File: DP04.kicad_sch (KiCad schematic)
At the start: 26 parts

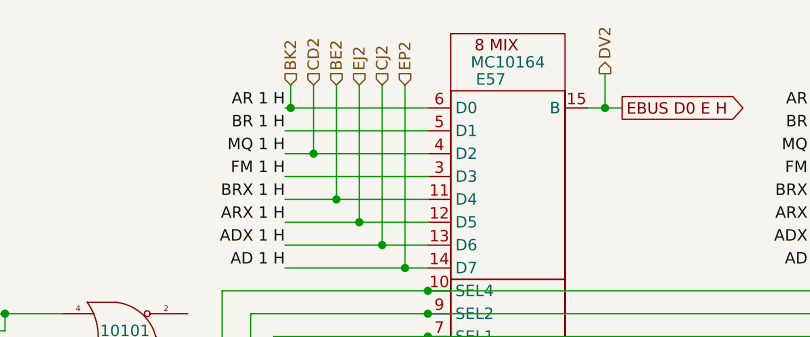
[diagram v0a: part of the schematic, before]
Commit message: Adding backplane connector slowly and painfully
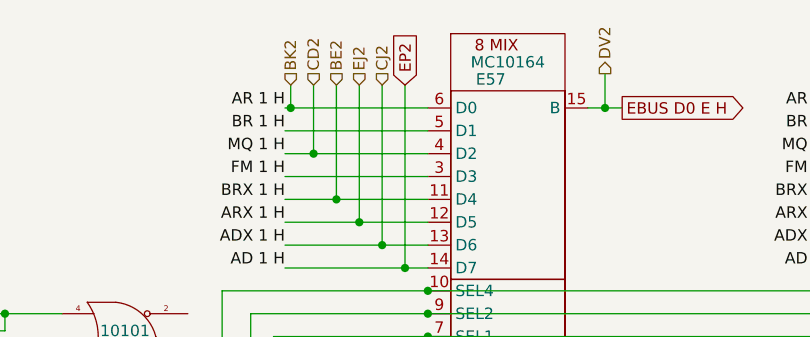
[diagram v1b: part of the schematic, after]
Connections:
- net DL1 renamed EP2
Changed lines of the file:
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@@
+    )
+  )
+  (global_label "EP2" (shape input) (at 85.09 39.37 90) (fields_autoplaced)
+    (effects (font (size 1.27 1.27)) (justify left))
+    (property "Intersheet References" "${INTERSHEET_REFS}" (id 0) (at 85.0106 33.3283 90)
+      (effects (font (size 1.27 1.27)) (justify left) hide)
     )
   )
@@
     (effects (font (size 1.27 1.27)) (justify right))
   )
-  (hierarchical_label "EP2" (shape input) (at 85.09 39.37 90)
-    (effects (font (size 1.27 1.27)) (justify left))
-  )
   (hierarchical_label "FD1" (shape input) (at 36.83 66.675 180)

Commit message: Convert all backplane refs to global labels and stick them on J1 pins. Convert all signal labels to global labels too so they are "global" inside M8512 board.
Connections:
- net AS1 renamed ARX 1 A H
- net AS2 renamed ARX 0 A H
- net BD2 renamed ARX 1 H
- net BK2 renamed AR 0 H
- net CJ2 renamed ADX 1 H
- net CP1 renamed AD 4 H
- net CR2 renamed CLK EDP 0 H
- net DC1 renamed ARX 2 H
- net DK1 renamed ADX 4 H
- net DR1 renamed AD 3 H
- net DR2 renamed AD 2 H
- net EBUS D0 E H renamed DV2
- net EBUS D1 E H renamed DS2
- net EBUS D2 E H renamed DT2
- net EBUS D3 E H renamed DP1
- net EBUS D4 E H renamed DP2
- net EBUS D5 E H renamed DU2
- net EF1 renamed DIAG READ FUNC 12 X H
- net EL1 renamed AD 5 H
- net EP2 renamed AD 1 H
- net ES1 renamed ADX 5 H
- net ET2 renamed ARX 5 A H
- net EU2 renamed ARX 3 A H
- net EV2 renamed ARX 4 A H
- net FA1 renamed DIAG 05 A H
- net FD1 renamed DIAG 04 A H
- net FE1 renamed DIAG 06 A H
- net FF2 renamed ARX 2 A H
- net FM1 renamed APR FM BLOCK 2 H
- net FN1 renamed APR FM ADR 4 H
- net FP1 renamed APR FM BLOCK 4 H
- net FP2 renamed APR FM ADR 1 H
- net FR1 renamed APR FM BLOCK 1 H
- net FR2 renamed APR FM ADR 10 H
- net FS1 renamed APR FM ADR 2 H

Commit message: Nearly done switching to <ABn> backplane labels
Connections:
- net ADX 1 H: no longer E57.13 (D6)
- net ARX 2 A H: no longer E61.6 (D3)
- net ARX 3 A H: no longer E63.12 (D0)
- net ARX 4 A H: no longer E63.11 (D1)
- net ARX 5 A H: no longer E63.9 (D2)
- net BR 1 H: no longer E57.5 (D1)
- net FM 0 H: now also E57.3 (D3)
- net FM 1 H: no longer E57.3 (D3)
- net AA1 renamed ARX 5 H <AA1>
- net AC1 renamed ARX 4 H <AC1>
- net AD 1 H renamed AD 0 H <EP2>
- net AD 0 H <EP2>: no longer E50.14 (D7)
- net AD 2 H renamed AD 2 H <DR2>
- net AD 3 H renamed AD 3 H <DR1>
- net AD 4 H renamed AD 4 H <CP1>
- net AD 5 H renamed AD 5 H <EL1>
- net ADX 4 H renamed ADX 4 H <DK1>
- net ADX 5 H renamed ADX 5 H <ES1>
- net AJ2 renamed ARX 3 H <AJ2>
- net APR FM ADR 1 H renamed APR FM ADR 1 H <FP2>
- net APR FM ADR 10 H renamed APR FM ADR 10 H <FR2>
- net APR FM ADR 2 H renamed APR FM ADR 2 H <FS1>
- net APR FM ADR 4 H renamed APR FM ADR 4 H <FN1>
- net APR FM BLOCK 1 H renamed APR FM BLOCK 1 H <FR1>
- net APR FM BLOCK 2 H renamed APR FM BLOCK 2 H <FM1>
- net APR FM BLOCK 4 H renamed APR FM BLOCK 4 H <FP1>
- net AR 0 H renamed AR 0 H <BK2>
- net AR 0 H <BK2>: no longer E50.6 (D0), E70.11 (D)
- net AR2 renamed CRAM BR LOAD A H <DJ2>
- net CRAM BR LOAD A H <DJ2>: no longer E11.10 (Cin)
- net ARX 0 A H renamed AR 0 A H <FJ2>
- net AR 0 A H <FJ2>: no longer E8.12 (D0)
- net ARX 1 A H renamed AR 1 A H <FC1>
- net AR 1 A H <FC1>: no longer E8.11 (D1)
- net ARX 1 H renamed ARX 0 H <EJ2>
- net ARX 0 H <EJ2>: no longer E50.12 (D5)
- net ARX 2 H renamed ARX 2 H <DC1>
- net BE2 renamed BRX 0 H <BE2>
- net BRX 0 H <BE2>: no longer E50.11 (D4), E8.15 (Q1)
- net BM2 renamed BR 0 H
- net BR 0 H: now also E57.5 (D1); no longer E61.14 (Q0)
- net CD2 renamed MQ 0 H <CD2>
- net MQ 0 H <CD2>: no longer E50.4 (D2)
- net CE2 renamed <CE2>
- net CLK EDP 0 H renamed CLK EDP 0 H <CR2>
- net CS1 renamed MQ 4 H <CS1>
- net DF1 renamed MQ 5 H <DF1>
- net DIAG 04 A H renamed DIAG 04 A H <FD1>
- net DIAG 05 A H renamed DIAG 05 A H <FA1>
- net DIAG 06 A H renamed DIAG 06 A H <FE1>
- net DIAG READ FUNC 12 X H renamed DIAG READ FUNC 12 X H <EF1>
- net DP1 renamed EBUS D3 E H <DP1>
- net DP2 renamed EBUS D4 E H <DP2>
- net DS2 renamed EBUS D1 E H <DS2>
- net DT2 renamed EBUS D2 E H <DT2>
- net DU2 renamed EBUS D5 E H <DU2>
- net DV2 renamed EBUS D0 E H <DV2>
- net EDP FM PARITY 0-5 H renamed EDP FM PARITY 0-5 H <FM2>
- net FE2 renamed FE2 <FE2>
- new net AD 1 H <DL1>: E50.14 (D7)
- new net ADX 0 H <CJ2>: E57.13 (D6)
- new net AR 1 H <BL2>: E50.6 (D0), E70.11 (D)
- new net AR 2 A H <FF2>: E61.6 (D3)
- new net AR 3 A H <EU2>: E63.12 (D0)
- new net AR 4 A H <EV2>: E63.11 (D1)
- new net AR 5 A H <ET2>: E63.9 (D2)
- new net ARX 0 A H <AS2>: E8.12 (D0)
- new net ARX 1 A H <AS1>: E8.11 (D1)
- new net ARX 1 H <BD2>: E50.12 (D5)
- new net BR 0 H <BM2>: E61.14 (Q0)
- new net BRX 1 H: E50.11 (D4), E8.15 (Q1)
- new net CRAM BRX LOAD A H <AR2>: E11.10 (Cin)
- new net MQ 1 H: E50.4 (D2)
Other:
- moved on the sheet: DL1, E10, E11C, E29A, E29B, E34A, E34B, E38C, E57, E58, E59A, E59B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

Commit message: Label BP connectors in EDP with their signal names.
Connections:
- net FE2 <FE2> renamed <FE2>
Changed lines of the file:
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@@
     )
   )
-  (global_label "FE2 <FE2>" (shape input) (at 50.8 96.52 180) (fields_autoplaced)
+  (global_label "<FE2>" (shape input) (at 50.8 96.52 180) (fields_autoplaced)
     (effects (font (size 1.27 1.27)) (justify right))
-    (property "Intersheet References" "${INTERSHEET_REFS}" (id 0) (at 37.3802 96.4406 0)
+    (property "Intersheet References" "${INTERSHEET_REFS}" (id 0) (at 41.795 96.4406 0)
       (effects (font (size 1.27 1.27)) (justify right) hide)
     )

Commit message: Fix a bunch of typos, add ${N} macros for slot specific net names
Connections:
- net AD 0 H <EP2> renamed AD ${N+0} H <EP2>
- net AD 1 H <DL1> renamed AD ${N+1} H <DL1>
- net AD 2 H <DR2> renamed AD ${N+2} H <DR2>
- net AD 3 H <DR1> renamed AD ${N+3} H <DR1>
- net AD 4 H <CP1> renamed AD ${N+4} H <CP1>
- net AD 5 H <EL1> renamed AD ${N+5} H <EL1>
- net ADX 0 H <CJ2> renamed ADX ${N+0} H <CJ2>
- net ADX 1 H renamed ADX ${N+1} H
- net ADX 2 H renamed ADX ${N+2} H
- net ADX 3 H renamed ADX ${N+3} H
- net ADX 4 H <DK1> renamed ADX ${N+4} H <DK1>
- net ADX 5 H <ES1> renamed ADX ${N+5} H <ES1>
- net AR 0 A H <FJ2> renamed AR ${N+0}A H <FJ2>
- net AR 0 H <BK2> renamed AR ${N+0} H <BK2>
- net AR 1 A H <FC1> renamed AR ${N+1} A H <FC1>
- net AR 1 H <BL2> renamed AR ${N+1} H <BL2>
- net AR 2 A H <FF2> renamed AR ${N+2} A H <FF2>
- net AR 2 H renamed AR ${N+2} H
- net AR 3 A H <EU2> renamed AR ${N+3} A H <EU2>
- net AR 3 H renamed AR ${N+3} H
- net AR 4 A H <EV2> renamed AR ${N+4} A H <EV2>
- net AR 4 H renamed AR ${N+4} H
- net AR 5 A H <ET2> renamed AR ${N+5} A H <ET2>
- net AR 5 H renamed AR ${N+5} H
- net ARX 0 A H <AS2> renamed ARX ${N+0} A H <AS2>
- net ARX 0 H <EJ2> renamed ARX ${N+0} H <EJ2>
- net ARX 1 A H <AS1> renamed ARX ${N+1} A H <AS1>
- net ARX 1 H <BD2> renamed ARX ${N+1} H <BD2>
- net ARX 2 A H renamed ARX ${N+2} A H
- net ARX 2 H <DC1> renamed ARX ${N+2} H <DC1>
- net ARX 3 A H renamed ARX ${N+3} A H
- net ARX 3 H <AJ2> renamed ARX ${N+3} H <AJ2>
- net ARX 4 A H renamed ARX ${N+4} A H
- net ARX 4 H <AC1> renamed ARX ${N+4} H <AC1>
- net ARX 5 A H renamed ARX ${N+5} A H
- net ARX 5 H <AA1> renamed ARX ${N+5} H <AA1>
- net BR 0 H renamed BR ${N+0} H
- net BR 0 H <BM2> renamed BR ${N+0} H <BM2>
- net BR 1 H renamed BR ${N+1} H
- net BR 2 H renamed BR ${N+2} H
- net BR 3 H renamed BR ${N+3} H
- net BR 4 H renamed BR ${N+4} H
- net BR 5 H renamed BR ${N+5} H
- net BRX 0 H <BE2> renamed BRX ${N+0} H <BE2>
- net BRX 1 H renamed BRX ${N+1} H
- net BRX 2 H renamed BRX ${N+2} H
- net BRX 3 H renamed BRX ${N+3} H
- net BRX 4 H renamed BRX ${N+4} H
- net BRX 5 H renamed BRX ${N+5} H
- net CLK EDP 0 DELAYED H renamed CLK EDP ${N+0} DELAYED H
- net CLK EDP 0 H <CR2> renamed CLK EDP ${N+0} H <CR2>
- net EBUS D0 E H <DV2> renamed EBUS D${N+0} E H <DV2>
- net EBUS D1 E H <DS2> renamed EBUS D${N+1} E H <DS2>
- net EBUS D2 E H <DT2> renamed EBUS D${N+2} E H <DT2>
- net EBUS D3 E H <DP1> renamed EBUS D${N+3} E H <DP1>
- net EBUS D4 E H <DP2> renamed EBUS D${N+4} E H <DP2>
- net EBUS D5 E H <DU2> renamed EBUS D${N+5} E H <DU2>
- net EDP FM PARITY 0-5 H <FM2> renamed EDP FM PARITY ${N+0}-${N+5} H <FM2>
- net FM 0 H renamed FM ${N+0} H
- net FM 1 H renamed FM ${N+1} H
- net FM 2 H renamed FM ${N+2} H
- net FM 3 H renamed FM ${N+3} H
- net FM 4 H renamed FM ${N+4} H
- net FM 5 H renamed FM ${N+5} H
- net MQ 0 H <CD2> renamed MQ ${N+0} H <CD2>
- net MQ 1 H renamed MQ ${N+1} H
- net MQ 2 H renamed MQ ${N+2} H
- net MQ 3 H renamed MQ ${N+3} H
- net MQ 4 H <CS1> renamed MQ ${N+4} H <CS1>
- net MQ 5 H <DF1> renamed MQ ${N+5} H <DF1>
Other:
- moved on the sheet: DL1, E11C, E29A, E29B, E38C, E58, E61, E63, E64, E65, E66A, E66B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
